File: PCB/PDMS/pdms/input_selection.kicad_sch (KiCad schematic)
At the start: 40 parts, among them U1 CPC1117N, U10 CPC1117N, U4 CPC1117N, U5 CPC1117N, U6 CPC1117N, U7 CPC1117N, U8 CPC1117N, U9 CPC1117N

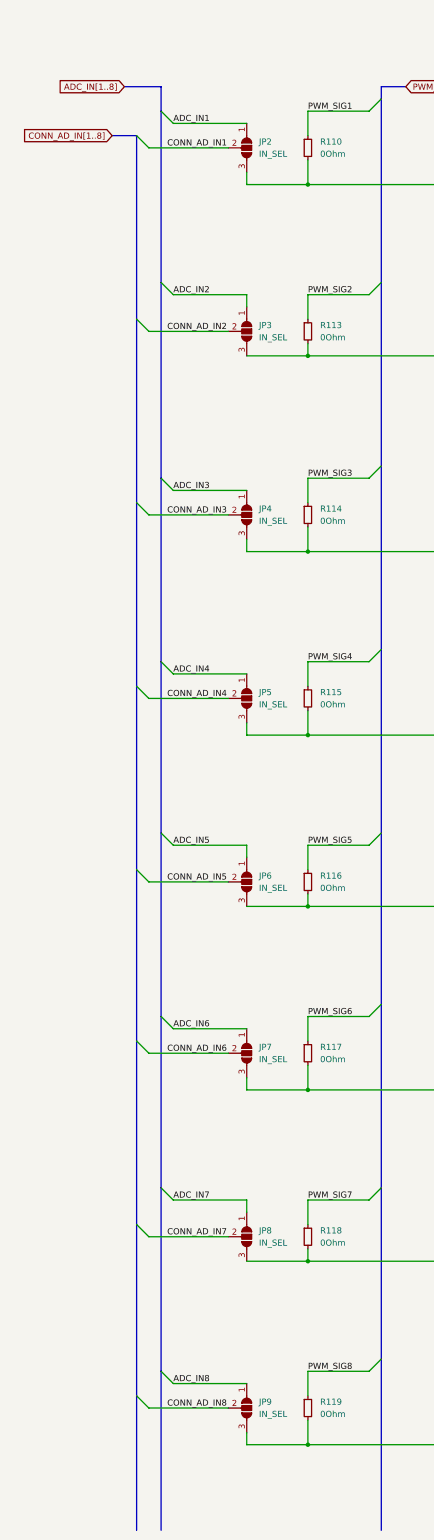
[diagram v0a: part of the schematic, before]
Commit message: ADC protection refactored - 73
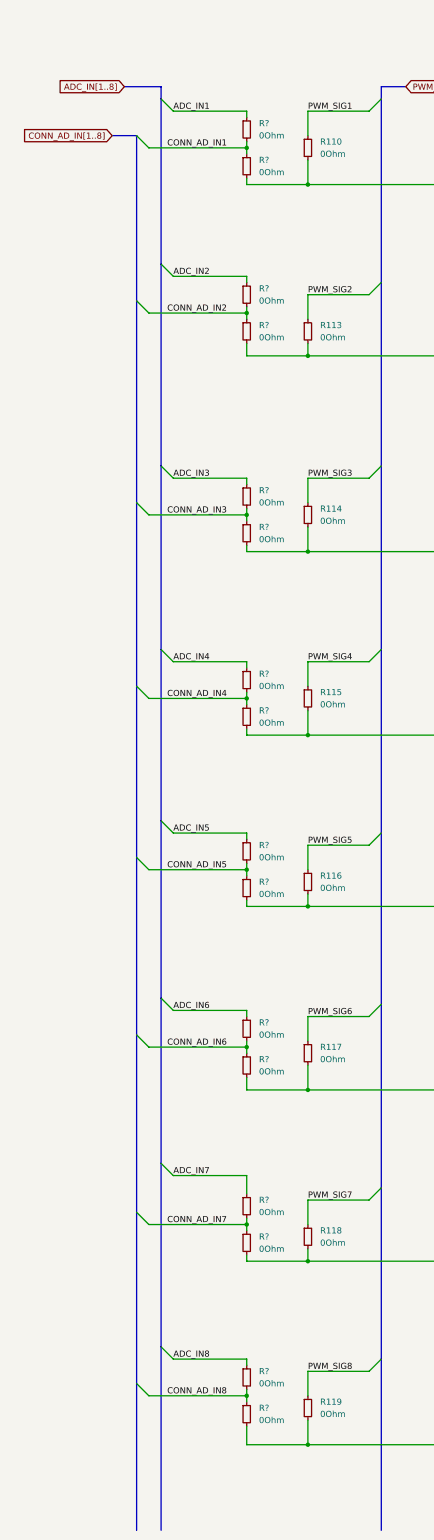
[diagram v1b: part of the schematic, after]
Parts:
- removed JP2, JP3, JP4, JP5, JP6, JP7, JP8, JP9: IN_SEL, Jumper:SolderJumper-3_P1.3mm_Open_Pad1.0x1.5mm, symbol Jumper:SolderJumper_3_Open
- added R? (x16): 0Ohm, Resistor_SMD:R_0402_1005Metric, symbol Device:R_Small
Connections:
- net ADC_IN1: now also R?.1
- net ADC_IN2: now also R?.1
- net ADC_IN3: now also R?.1
- net ADC_IN4: now also R?.1
- net ADC_IN5: now also R?.1
- net ADC_IN6: now also R?.1
- net ADC_IN7: now also R?.1
- net ADC_IN8: now also R?.1
- net CONN_AD_IN1: now also R?.1, R?.2
- net CONN_AD_IN2: now also R?.1, R?.2
- net CONN_AD_IN3: now also R?.1, R?.2
- net CONN_AD_IN4: now also R?.1, R?.2
- net CONN_AD_IN5: now also R?.1, R?.2
- net CONN_AD_IN6: now also R?.1, R?.2
- net CONN_AD_IN7: now also R?.1, R?.2
- net CONN_AD_IN8: now also R?.1, R?.2
- net at R110.2, R111.2, U1.3: now also R?.2
- net at R114.2, R121.2, U5.3: now also R?.2
- net at R119.2, R126.2, U10.3: now also R?.2
- net at R116.2, R123.2, U7.3: now also R?.2
- net at R117.2, R124.2, U8.3: now also R?.2
- net at R113.2, R120.2, U4.3: now also R?.2
- net at R115.2, R122.2, U6.3: now also R?.2
- net at R118.2, R125.2, U9.3: now also R?.2

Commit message: Safety finished - 53
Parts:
- gave numbers to parts that had none: 16
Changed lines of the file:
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@@
   (symbol (lib_id "Device:R_Small") (at 119.38 181.61 0) (unit 1)
     (in_bom yes) (on_board yes) (fields_autoplaced)
-    (property "Reference" "R?" (id 0) (at 121.92 180.3399 0)
+    (property "Reference" "R107" (id 0) (at 121.92 180.3399 0)
       (effects (font (size 1.27 1.27)) (justify left))
     )
@@
   (symbol (lib_id "Device:R_Small") (at 119.38 209.55 0) (unit 1)
     (in_bom yes) (on_board yes) (fields_autoplaced)
-    (property "Reference" "R?" (id 0) (at 121.92 208.2799 0)
+    (property "Reference" "R159" (id 0) (at 121.92 208.2799 0)
       (effects (font (size 1.27 1.27)) (justify left))
     )
@@
   (symbol (lib_id "Device:R_Small") (at 119.38 101.6 0) (unit 1)
     (in_bom yes) (on_board yes) (fields_autoplaced)
-    (property "Reference" "R?" (id 0) (at 121.92 100.3299 0)
+    (property "Reference" "R90" (id 0) (at 121.92 100.3299 0)
       (effects (font (size 1.27 1.27)) (justify left))
     )
@@
   (symbol (lib_id "Device:R_Small") (at 119.38 67.31 0) (unit 1)
     (in_bom yes) (on_board yes) (fields_autoplaced)
-    (property "Reference" "R?" (id 0) (at 121.92 66.0399 0)
+    (property "Reference" "R88" (id 0) (at 121.92 66.0399 0)
       (effects (font (size 1.27 1.27)) (justify left))
     )
@@
   (symbol (lib_id "Device:R_Small") (at 119.38 59.69 0) (unit 1)
     (in_bom yes) (on_board yes) (fields_autoplaced)
-    (property "Reference" "R?" (id 0) (at 121.92 58.4199 0)
+    (property "Reference" "R87" (id 0) (at 121.92 58.4199 0)
       (effects (font (size 1.27 1.27)) (justify left))
     )
@@
   (symbol (lib_id "Device:R_Small") (at 119.38 290.83 0) (unit 1)
     (in_bom yes) (on_board yes) (fields_autoplaced)
-    (property "Reference" "R?" (id 0) (at 121.92 289.5599 0)
+    (property "Reference" "R164" (id 0) (at 121.92 289.5599 0)
       (effects (font (size 1.27 1.27)) (justify left))
     )
@@
   (symbol (lib_id "Device:R_Small") (at 119.38 318.77 0) (unit 1)
     (in_bom yes) (on_board yes) (fields_autoplaced)
-    (property "Reference" "R?" (id 0) (at 121.92 317.4999 0)
+    (property "Reference" "R165" (id 0) (at 121.92 317.4999 0)
       (effects (font (size 1.27 1.27)) (justify left))
     )
@@
   (symbol (lib_id "Device:R_Small") (at 119.38 173.99 0) (unit 1)
     (in_bom yes) (on_board yes) (fields_autoplaced)
-    (property "Reference" "R?" (id 0) (at 121.92 172.7199 0)
+    (property "Reference" "R106" (id 0) (at 121.92 172.7199 0)
       (effects (font (size 1.27 1.27)) (justify left))
     )
@@
   (symbol (lib_id "Device:R_Small") (at 119.38 283.21 0) (unit 1)
     (in_bom yes) (on_board yes) (fields_autoplaced)
-    (property "Reference" "R?" (id 0) (at 121.92 281.9399 0)
+    (property "Reference" "R163" (id 0) (at 121.92 281.9399 0)
       (effects (font (size 1.27 1.27)) (justify left))
     )
@@
   (symbol (lib_id "Device:R_Small") (at 119.38 326.39 0) (unit 1)
     (in_bom yes) (on_board yes) (fields_autoplaced)
-    (property "Reference" "R?" (id 0) (at 121.92 325.1199 0)
+    (property "Reference" "R166" (id 0) (at 121.92 325.1199 0)
       (effects (font (size 1.27 1.27)) (justify left))
     )
@@
   (symbol (lib_id "Device:R_Small") (at 119.38 246.38 0) (unit 1)
     (in_bom yes) (on_board yes) (fields_autoplaced)
-    (property "Reference" "R?" (id 0) (at 121.92 245.1099 0)
+    (property "Reference" "R161" (id 0) (at 121.92 245.1099 0)
       (effects (font (size 1.27 1.27)) (justify left))
     )
@@
   (symbol (lib_id "Device:R_Small") (at 119.38 217.17 0) (unit 1)
     (in_bom yes) (on_board yes) (fields_autoplaced)
-    (property "Reference" "R?" (id 0) (at 121.92 215.8999 0)
+    (property "Reference" "R160" (id 0) (at 121.92 215.8999 0)
       (effects (font (size 1.27 1.27)) (justify left))
     )
@@
   (symbol (lib_id "Device:R_Small") (at 119.38 143.51 0) (unit 1)
     (in_bom yes) (on_board yes) (fields_autoplaced)
-    (property "Reference" "R?" (id 0) (at 121.92 142.2399 0)
+    (property "Reference" "R92" (id 0) (at 121.92 142.2399 0)
       (effects (font (size 1.27 1.27)) (justify left))
     )
@@
   (symbol (lib_id "Device:R_Small") (at 119.38 135.89 0) (unit 1)
     (in_bom yes) (on_board yes) (fields_autoplaced)
-    (property "Reference" "R?" (id 0) (at 121.92 134.6199 0)
+    (property "Reference" "R91" (id 0) (at 121.92 134.6199 0)
       (effects (font (size 1.27 1.27)) (justify left))
     )
@@
   (symbol (lib_id "Device:R_Small") (at 119.38 93.98 0) (unit 1)
     (in_bom yes) (on_board yes) (fields_autoplaced)
-    (property "Reference" "R?" (id 0) (at 121.92 92.7099 0)
+    (property "Reference" "R89" (id 0) (at 121.92 92.7099 0)
       (effects (font (size 1.27 1.27)) (justify left))
     )
@@
   (symbol (lib_id "Device:R_Small") (at 119.38 254 0) (unit 1)
     (in_bom yes) (on_board yes) (fields_autoplaced)
-    (property "Reference" "R?" (id 0) (at 121.92 252.7299 0)
-      (effects (font (size 1.27 1.27)) (justify left))
-    )
+    (property "Reference" "R162" (id 0) (at 121.92 252.7299 0)
+      (effects (font (size 1.27 1.27)) (justify left))
+    )

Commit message: Final touch PDMS
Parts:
- added R? (x2): 1k, Resistor_SMD:R_0402_1005Metric, symbol Device:R_Small
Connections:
- net GND: now also R?.2
- net SAFETY_IN: now also R?.1, R?.1
- new net +5V: R?.2
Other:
- note added: "OPTIONAL"
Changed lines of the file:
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@@
   (junction (at 119.38 63.5) (diameter 0) (color 0 0 0 0)
   )
+  (junction (at 250.19 59.055) (diameter 0) (color 0 0 0 0)
+  )
   (junction (at 175.26 71.12) (diameter 0) (color 0 0 0 0)
   )
@@
     (stroke (width 0) (type default) (color 0 0 0 0))
   )
+  (polyline (pts (xy 243.84 44.45) (xy 260.985 44.45))
+    (stroke (width 0) (type default) (color 0 0 0 0))
+  )
   (wire (pts (xy 175.26 147.32) (xy 177.8 147.32))
     (stroke (width 0) (type default) (color 0 0 0 0))
@@
     (stroke (width 0) (type default) (color 0 0 0 0))
   )
+  (wire (pts (xy 255.27 57.785) (xy 255.27 59.055))
+    (stroke (width 0) (type default) (color 0 0 0 0))
+  )
   (bus (pts (xy 96.52 247.65) (xy 96.52 284.48))
     (stroke (width 0) (type default) (color 0 0 0 0))
@@
     (stroke (width 0) (type default) (color 0 0 0 0))
   )
+  (wire (pts (xy 250.19 51.435) (xy 250.19 52.705))
+    (stroke (width 0) (type default) (color 0 0 0 0))
+  )
   (wire (pts (xy 119.38 294.64) (xy 132.08 294.64))
     (stroke (width 0) (type default) (color 0 0 0 0))
@@
     (stroke (width 0) (type default) (color 0 0 0 0))
   )
+  (wire (pts (xy 250.19 59.055) (xy 255.27 59.055))
+    (stroke (width 0) (type default) (color 0 0 0 0))
+  )
   (wire (pts (xy 177.8 165.1) (xy 177.8 167.64))
     (stroke (width 0) (type default) (color 0 0 0 0))
@@
     (stroke (width 0) (type default) (color 0 0 0 0))
   )
+  (polyline (pts (xy 260.985 44.45) (xy 260.985 62.865))
+    (stroke (width 0) (type default) (color 0 0 0 0))
+  )
   (wire (pts (xy 175.26 185.42) (xy 177.8 185.42))
     (stroke (width 0) (type default) (color 0 0 0 0))
@@
     (stroke (width 0) (type default) (color 0 0 0 0))
   )
+  (polyline (pts (xy 243.84 44.45) (xy 243.84 62.865))
+    (stroke (width 0) (type default) (color 0 0 0 0))
+  )
   (wire (pts (xy 104.14 276.86) (xy 119.38 276.86))
     (stroke (width 0) (type default) (color 0 0 0 0))
   )
+  (polyline (pts (xy 260.985 62.865) (xy 243.84 62.865))
+    (stroke (width 0) (type default) (color 0 0 0 0))
+  )
   (wire (pts (xy 182.88 238.76) (xy 182.88 241.3))
     (stroke (width 0) (type default) (color 0 0 0 0))
@@
     (stroke (width 0) (type default) (color 0 0 0 0))
   )
+  (wire (pts (xy 243.205 59.055) (xy 250.19 59.055))
+    (stroke (width 0) (type default) (color 0 0 0 0))
+  )
   (wire (pts (xy 144.78 132.08) (xy 132.08 132.08))
     (stroke (width 0) (type default) (color 0 0 0 0))
@@
     (stroke (width 0) (type default) (color 0 0 0 0))
   )
+  (wire (pts (xy 250.19 57.785) (xy 250.19 59.055))
+    (stroke (width 0) (type default) (color 0 0 0 0))
+  )
   (bus (pts (xy 96.52 175.26) (xy 96.52 210.82))
     (stroke (width 0) (type default) (color 0 0 0 0))
@@
     (stroke (width 0) (type default) (color 0 0 0 0))
   )
+  (wire (pts (xy 255.27 51.435) (xy 255.27 52.705))
+    (stroke (width 0) (type default) (color 0 0 0 0))
+  )
   (wire (pts (xy 190.5 312.42) (xy 187.96 312.42))
     (stroke (width 0) (type default) (color 0 0 0 0))
@@
   (wire (pts (xy 132.08 317.5) (xy 132.08 322.58))
     (stroke (width 0) (type default) (color 0 0 0 0))
+  )
+  (text "OPTIONAL" (at 243.84 43.815 0)
+    (effects (font (size 1.27 1.27)) (justify left bottom))
   )
   (text "Remember about pull down if safety future is used!"
@@
     )
   )
+  (global_label "SAFETY_IN" (shape input) (at 243.205 59.055 180) (fields_autoplaced)
+    (effects (font (size 1.27 1.27)) (justify right))
+    (property "Intersheet References" "${INTERSHEET_REFS}" (id 0) (at 231.2971 59.1344 0)
+      (effects (font (size 1.27 1.27)) (justify right) hide)
+    )
+  )
   (global_label "SIG_IN[1..8]" (shape input) (at 208.28 50.8 0) (fields_autoplaced)
     (effects (font (size 1.27 1.27)) (justify left))
@@
     )
   )
+  (symbol (lib_id "Device:R_Small") (at 255.27 55.245 180) (unit 1)
+    (in_bom yes) (on_board yes)
+    (property "Reference" "R?" (id 0) (at 257.175 56.515 90)
+      (effects (font (size 1.27 1.27)) (justify right))
+    )
+    (property "Value" "1k" (id 1) (at 259.08 56.515 90)
+      (effects (font (size 1.27 1.27)) (justify right))
+    )
+    (property "Footprint" "Resistor_SMD:R_0402_1005Metric" (id 2) (at 255.27 55.245 0)
+      (effects (font (size 1.27 1.27)) hide)
+    )
+    (property "Datasheet" "~" (id 3) (at 255.27 55.245 0)
+      (effects (font (size 1.27 1.27)) hide)
+    )
+    (pin "1")
+    (pin "2")
+  )
   (symbol (lib_id "Device:R_Small") (at 180.34 335.28 270) (unit 1)
     (in_bom yes) (on_board yes)
@@
     (pin "4")
   )
+  (symbol (lib_id "power:+5V") (at 250.19 51.435 0) (unit 1)
+    (in_bom yes) (on_board yes) (fields_autoplaced)
+    (property "Reference" "#PWR?" (id 0) (at 250.19 55.245 0)
+      (effects (font (size 1.27 1.27)) hide)
+    )
+    (property "Value" "+5V" (id 1) (at 250.19 46.355 0))
+    (property "Footprint" "" (id 2) (at 250.19 51.435 0)
+      (effects (font (size 1.27 1.27)) hide)
+    )
+    (property "Datasheet" "" (id 3) (at 250.19 51.435 0)
+      (effects (font (size 1.27 1.27)) hide)
+    )
+    (pin "1")
+  )
   (symbol (lib_id "power:GND") (at 177.8 165.1 180) (unit 1)
     (in_bom yes) (on_board yes)
@@
     (pin "2")
   )
+  (symbol (lib_id "power:GND") (at 255.27 51.435 180) (unit 1)
+    (in_bom yes) (on_board yes) (fields_autoplaced)
+    (property "Reference" "#PWR?" (id 0) (at 255.27 45.085 0)
+      (effects (font (size 1.27 1.27)) hide)
+    )
+    (property "Value" "GND" (id 1) (at 255.27 46.355 0))
+    (property "Footprint" "" (id 2) (at 255.27 51.435 0)
+      (effects (font (size 1.27 1.27)) hide)
+    )
+    (property "Datasheet" "" (id 3) (at 255.27 51.435 0)
+      (effects (font (size 1.27 1.27)) hide)
+    )
+    (pin "1")
+  )
   (symbol (lib_id "Device:R_Small") (at 119.38 173.99 0) (unit 1)
     (in_bom yes) (on_board yes) (fields_autoplaced)
@@
       (effects (font (size 1.27 1.27)) hide)
     )
+    (pin "1")
+    (pin "2")
+  )
+  (symbol (lib_id "Device:R_Small") (at 250.19 55.245 180) (unit 1)
+    (in_bom yes) (on_board yes)
+    (property "Reference" "R?" (id 0) (at 245.11 56.515 90)
+      (effects (font (size 1.27 1.27)) (justify right))
+    )
+    (property "Value" "1k" (id 1) (at 247.015 56.515 90)
+      (effects (font (size 1.27 1.27)) (justify right))
+    )
+    (property "Footprint" "Resistor_SMD:R_0402_1005Metric" (id 2) (at 250.19 55.245 0)
+      (effects (font (size 1.27 1.27)) hide)
+    )
+    (property "Datasheet" "~" (id 3) (at 250.19 55.245 0)
+      (effects (font (size 1.27 1.27)) hide)
+    )

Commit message: Sitched via side
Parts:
- gave numbers to parts that had none: 2
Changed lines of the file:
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@@
   (symbol (lib_id "Device:R_Small") (at 255.27 55.245 180) (unit 1)
     (in_bom yes) (on_board yes)
-    (property "Reference" "R?" (id 0) (at 257.175 56.515 90)
+    (property "Reference" "R170" (id 0) (at 257.175 56.515 90)
       (effects (font (size 1.27 1.27)) (justify right))
     )
@@
   (symbol (lib_id "power:+5V") (at 250.19 51.435 0) (unit 1)
     (in_bom yes) (on_board yes) (fields_autoplaced)
-    (property "Reference" "#PWR?" (id 0) (at 250.19 55.245 0)
+    (property "Reference" "#PWR0383" (id 0) (at 250.19 55.245 0)
       (effects (font (size 1.27 1.27)) hide)
     )
@@
   (symbol (lib_id "power:GND") (at 255.27 51.435 180) (unit 1)
     (in_bom yes) (on_board yes) (fields_autoplaced)
-    (property "Reference" "#PWR?" (id 0) (at 255.27 45.085 0)
+    (property "Reference" "#PWR0379" (id 0) (at 255.27 45.085 0)
       (effects (font (size 1.27 1.27)) hide)
     )
@@
   (symbol (lib_id "Device:R_Small") (at 250.19 55.245 180) (unit 1)
     (in_bom yes) (on_board yes)
-    (property "Reference" "R?" (id 0) (at 245.11 56.515 90)
-      (effects (font (size 1.27 1.27)) (justify right))
-    )
+    (property "Reference" "R169" (id 0) (at 245.11 56.515 90)
+      (effects (font (size 1.27 1.27)) (justify right))
+    )

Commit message: Major changes with new switch
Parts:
- removed U1, U10, U4, U5, U6, U7, U8, U9: CPC1117N, Package_SO:SOP-4_3.8x4.1mm_P2.54mm, symbol Relay_SolidState:CPC1117N
- added U1, U10, U4, U5, U6, U7, U8, U9: AQY221R4VY, PDMS_Additional:SOTFL127P485X190-4N, symbol pdms_additional:AQY221R4VY
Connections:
- net GND: now also U1.2 (K), U10.2 (K), U4.2 (K), U5.2 (K), U6.2 (K), U7.2 (K), U8.2 (K), U9.2 (K)
- net SIG_IN1: now also U1.3 (D1)
- net SIG_IN2: now also U4.3 (D1)
- net SIG_IN3: now also U5.3 (D1)
- net SIG_IN4: now also U6.3 (D1)
- net SIG_IN5: now also U7.3 (D1)
- net SIG_IN6: now also U8.3 (D1)
- net SIG_IN7: now also U9.3 (D1)
- net SIG_IN8: now also U10.3 (D1)
- net at R119.2, R126.2, R166.2: now also U10.4 (D2)
- net at R132.1: now also U9.1 (A)
- net at R116.2, R123.2, R160.2: now also U7.4 (D2)
- net at R131.1: now also U8.1 (A)
- net at R107.2, R115.2, R122.2: now also U6.4 (D2)
- net at R113.2, R120.2, R90.2: now also U4.4 (D2)
- net at R110.2, R111.2, R88.2: now also U1.4 (D2)
- net at R133.1: now also U10.1 (A)
- net at R112.1: now also U1.1 (A)
- net at R128.1: now also U5.1 (A)
- net at R130.1: now also U7.1 (A)
- net at R114.2, R121.2, R92.2: now also U5.4 (D2)
- net at R118.2, R125.2, R164.2: now also U9.4 (D2)
- net at R117.2, R124.2, R162.2: now also U8.4 (D2)
- net at R129.1: now also U6.1 (A)
- net at R127.1: now also U4.1 (A)
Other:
- note added: "For 5V it should be around 386 Ohms If = <5 to 30mA>"
- note added: "Resistance should be selected for correct safety line voltage"
- note added: "https://www.mouser.pl/ProductDetail/Panasonic-Industrial-Devices/AQY221R4VY?qs=St27ATL478uV4j9hHKsfjA%3D%3D"
- moved on the sheet: R111, R112, R120, R121, R122, R123, R124, R125, R126, R127, R128, R129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
